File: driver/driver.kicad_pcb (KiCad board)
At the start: 2 copper layers, 48 x 34 mm, 25 parts, among them J1 Conn_02x08_Odd_Even_Male, J2 Conn_02x08_Odd_Even_Female, J3 Conn_01x05, J4 Conn_01x03_Pin, U1 DRV8804PWP, U2 SN74HCS165DYYR

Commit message: Setup over USB
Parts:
- moved C3 6.79 mm to (136.2, 78.0)
- moved R5 6.79 mm to (134.1, 78.3)
- moved R6 6.79 mm to (132.5, 77.6)
- moved U2 6.79 mm to (135.2, 74.8)
- moved J4 6.24 mm to (135.2, 81.5)
- moved D2 5.47 mm to (108.4, 82.5)
- moved D3 3.97 mm to (113.4, 82.5)
- moved R1 3.56 mm to (110.9, 82.2), turned to 0 degrees
- moved D4 2.44 mm to (118.5, 82.5)
- moved R2 2.34 mm to (115.9, 82.2), turned to 0 degrees
- moved C1 2.23 mm to (120.5, 73.2)
- moved C2 2.23 mm to (118.5, 72.2)
- moved D1 2.23 mm to (114.0, 73.2)
- moved U1 2.23 mm to (124.1, 71.2)
- moved R4 2.12 mm to (125.9, 82.2), turned to 0 degrees
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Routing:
- net FAULT: track 0.00 -> 41.4 mm, vias 0 -> 1
- net SCLK: track 56.4 -> 65.5 mm
- net CI: track 19.2 -> 26.4 mm
- net PO: track 36.2 -> 43.3 mm
- net LOAD: track 37.5 -> 43.7 mm
- net LATCH: track 39.4 -> 41.6 mm
- net NENBL: track 49.7 -> 51.9 mm
- net CO: track 19.6 -> 21.8 mm
- net Net-(U1-VCLAMP): track 14.2 -> 12.0 mm
- net PI: track 16.7 -> 18.9 mm
- net Net-(D5-Pad1): track 1.53 -> 0.00 mm
- net Net-(D4-Pad1): track 1.53 -> 0.00 mm
- net Net-(D3-Pad1): track 1.53 -> 0.00 mm
- net Net-(D2-Pad1): track 1.53 -> 0.00 mm
- net Net-(J3-Pin_4): track 14.1 -> 15.6 mm
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
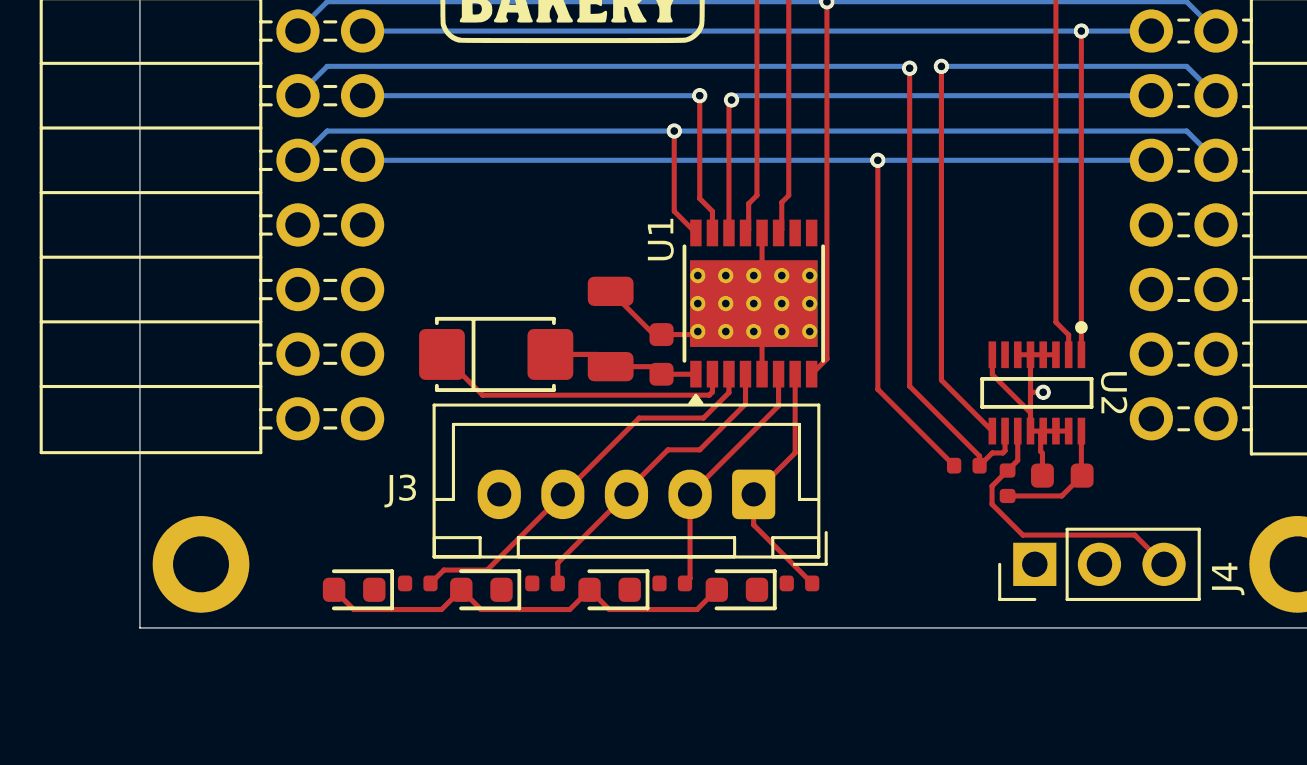
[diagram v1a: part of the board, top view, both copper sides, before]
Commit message: Make glyph list configurable.
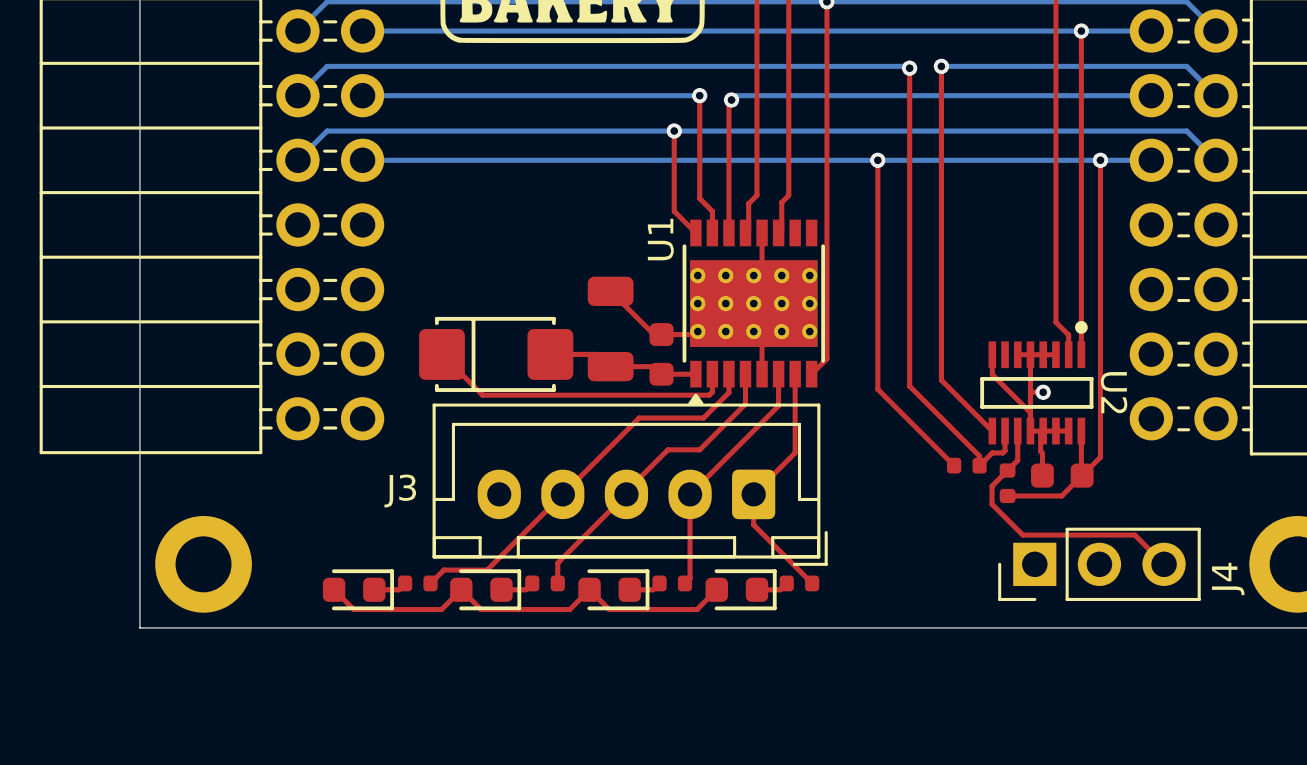
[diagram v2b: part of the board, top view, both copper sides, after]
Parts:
- moved H3 0.10 mm to (102.5, 81.5)
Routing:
- net +3V3: track 49.3 -> 62.0 mm, vias 1 -> 2
- net Net-(D3-Pad1): track 0.00 -> 1.31 mm
- net Net-(D2-Pad1): track 0.00 -> 1.31 mm
- net Net-(D5-Pad1): track 0.00 -> 1.27 mm
- net Net-(D4-Pad1): track 0.00 -> 1.27 mm
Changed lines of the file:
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@@
 		(locked yes)
 		(layer "F.Cu")
-		(at 102.4 81.5)
+		(at 102.5 81.5)
 		(descr "Mounting Hole 2.2mm, M2, generated by kicad-footprint-generator mountinghole.py")
 		(tags "mountinghole M2 ISO14580")
@@
 	)
 	(segment
+		(start 110.17 82.5)
+		(end 110.42 82.25)
+		(width 0.2)
+		(layer "F.Cu")
+		(net 9)
+	)
+	(segment
+		(start 109.21 82.5)
+		(end 110.17 82.5)
+		(width 0.2)
+		(layer "F.Cu")
+		(net 9)
+	)
+	(segment
 		(start 121.621 82.049)
 		(end 121.42 82.25)
@@
 		(layer "F.Cu")
 		(net 12)
+	)
+	(segment
+		(start 115.17 82.5)
+		(end 115.42 82.25)
+		(width 0.2)
+		(layer "F.Cu")
+		(net 13)
+	)
+	(segment
+		(start 114.21 82.5)
+		(end 115.17 82.5)
+		(width 0.2)
+		(layer "F.Cu")
+		(net 13)
+	)
+	(segment
+		(start 120.17 82.5)
+		(end 120.42 82.25)
+		(width 0.2)
+		(layer "F.Cu")
+		(net 14)
+	)
+	(segment
+		(start 119.25 82.5)
+		(end 120.17 82.5)
+		(width 0.2)
+		(layer "F.Cu")
+		(net 14)
+	)
+	(segment
+		(start 124.25 82.5)
+		(end 125.17 82.5)
+		(width 0.2)
+		(layer "F.Cu")
+		(net 15)
+	)
+	(segment
+		(start 125.17 82.5)
+		(end 125.42 82.25)
+		(width 0.2)
+		(layer "F.Cu")
+		(net 15)
 	)
 	(segment
@@
 	)
 	(segment
+		(start 137.75 77.292499)
+		(end 137.75 65.62)
+		(width 0.2)
+		(layer "F.Cu")
+		(net 19)
+	)
+	(segment
 		(start 129 65.62)
 		(end 129 74.622501)
@@
 	)
 	(segment
+		(start 137.029999 78.0125)
+		(end 137.75 77.292499)
+		(width 0.2)
+		(layer "F.Cu")
+		(net 19)
+	)
+	(segment
 		(start 136.999999 76.2625)
 		(end 136.999999 77.9825)
@@
 		(width 0.2)
 		(layer "F.Cu")
+		(net 19)
+	)
+	(via
+		(at 137.75 65.62)
+		(size 0.6)
+		(drill 0.3)
+		(layers "F.Cu" "B.Cu")
 		(net 19)
 	)
@@
 	)
 	(segment
+		(start 137.75 65.62)
+		(end 139.75 65.62)
+		(width 0.2)
+		(layer "B.Cu")
+		(net 19)
+	)
+	(segment
 		(start 129 65.62)
-		(end 139.75 65.62)
+		(end 137.75 65.62)
 		(width 0.2)
 		(layer "B.Cu")
